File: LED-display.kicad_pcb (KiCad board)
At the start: 2 copper layers, 96.5 x 49.5 mm, 85 parts, among them J1 Conn_01x01_Male, J10 Conn_01x01_Male, J11 Conn_01x01_Male, J12 Conn_01x01_Male, J13 Conn_01x01_Male, J14 Conn_01x01_Male, J2 Conn_01x01_Male, J3 Conn_01x01_Male, J4 Conn_01x01_Male, J5 Conn_01x01_Male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

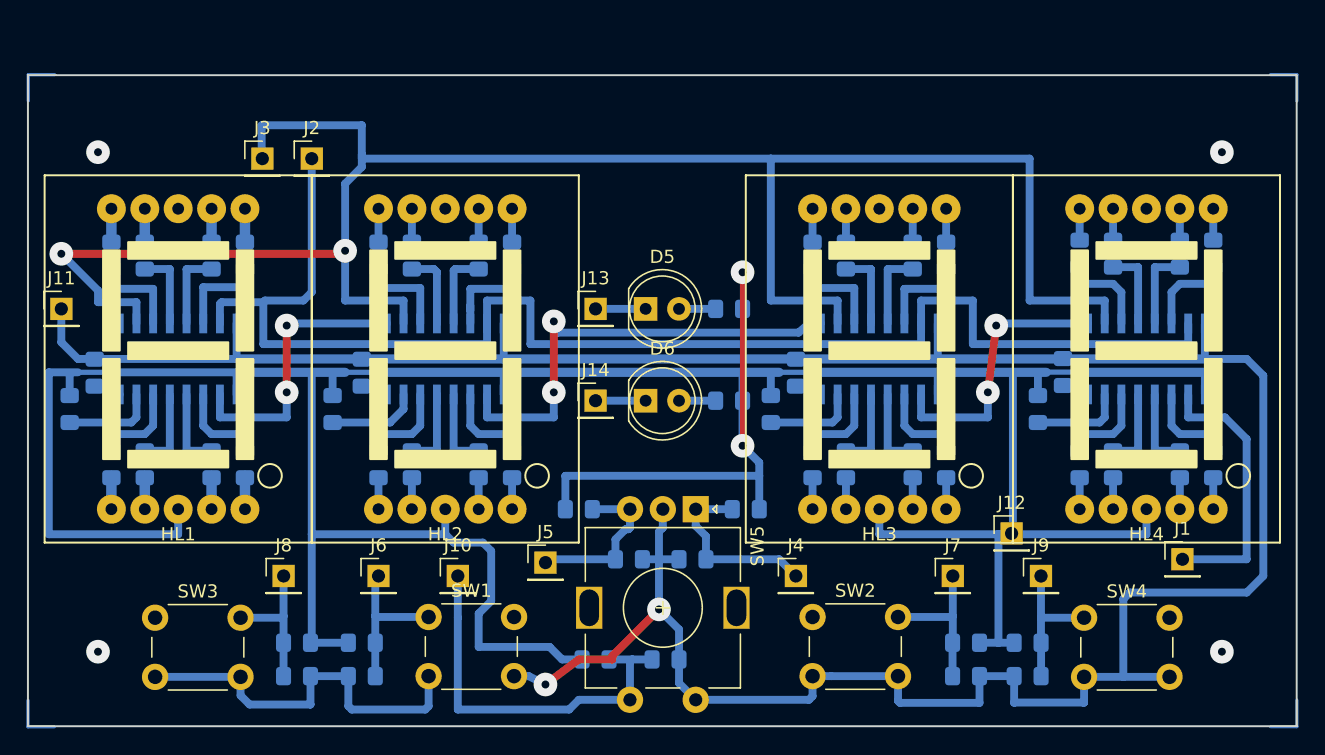
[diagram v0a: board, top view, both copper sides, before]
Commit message: Move buttons
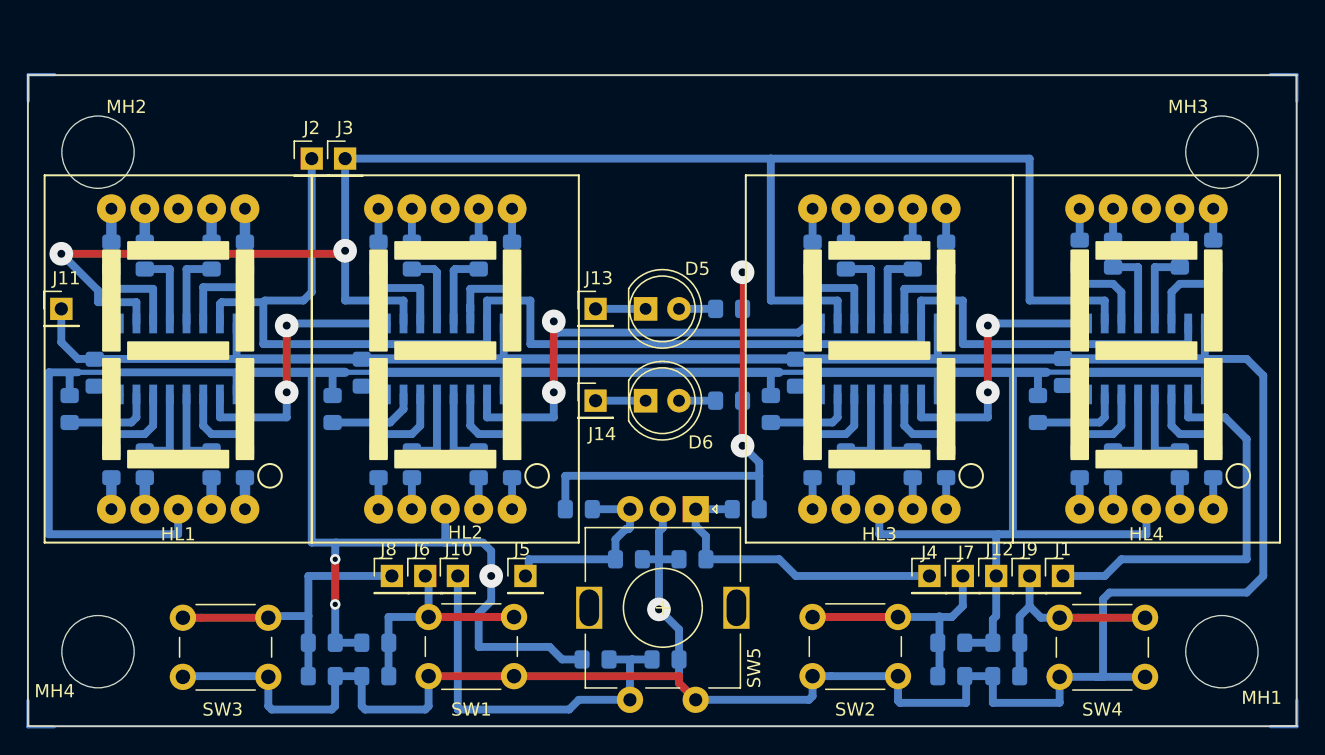
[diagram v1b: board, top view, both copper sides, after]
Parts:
- added MH1: MountingHole, MountingHole:MountingHole_5.5mm, F.Cu at (181.0, 84.5)
- added MH2: MountingHole, MountingHole:MountingHole_5.5mm, F.Cu at (95.5, 46.5)
- added MH3: MountingHole, MountingHole:MountingHole_5.5mm, F.Cu at (181.0, 46.5)
- added MH4: MountingHole, MountingHole:MountingHole_5.5mm, F.Cu at (95.5, 84.5)
- moved J4 10.2 mm to (158.8, 78.7)
- moved J1 9.18 mm to (168.9, 78.7)
- moved J8 8.23 mm to (117.9, 78.7)
- moved J3 6.30 mm to (114.3, 47.0)
- moved J6 3.56 mm to (120.4, 78.7)
- moved J12 3.44 mm to (163.8, 78.7)
- moved SW3 2.11 mm to (102.0, 81.9)
- moved C5 1.88 mm to (112.5, 86.4)
- moved R41 1.88 mm to (112.5, 83.8)
- moved SW4 1.86 mm to (168.7, 81.9)
- moved J5 1.83 mm to (128.0, 78.7)
- moved C6 1.63 mm to (164.6, 86.4)
- moved R42 1.62 mm to (164.6, 83.8)
- moved C4 1.12 mm to (160.4, 86.4)
- moved R40 1.12 mm to (160.4, 83.8)
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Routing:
- net /Zoom: track 10.9 -> 23.8 mm
- net /Latch: track 148.3 -> 136.0 mm
- net /Plus: track 14.3 -> 24.4 mm
- net /Data: track 20.9 -> 30.5 mm
- net /Min: track 11.8 -> 18.6 mm
- net /Rsrv: track 10.9 -> 17.1 mm
- net GND: track 245.6 -> 251.6 mm, vias 2 -> 1
- net /Hour: track 11.8 -> 17.2 mm
- net /Minus: track 12.6 -> 15.1 mm
- net VCC: track 272.9 -> 271.6 mm, vias 2 -> 5
- net Net-(D3-Pad2): track 20.9 -> 21.7 mm
- net (no net): vias 4 -> 0

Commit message: Small fixes
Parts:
- removed R46, R47, R48, R49: 0, Resistor_SMD:R_0805_2012Metric_Pad1.15x1.40mm_HandSolder
- added J15: PWM, Connector_PinHeader_2.54mm:PinHeader_1x01_P2.54mm_Vertical, F.Cu at (127.0, 44.5)
- J1: value Conn_01x01_Male -> Data
- J11: value Conn_01x01_Male -> Gnd
- J12: value Conn_01x01_Male -> Vcc
- J2: value Conn_01x01_Male -> Clock
- J3: value Conn_01x01_Male -> Latch
- R44, R45: moved to F.Cu
- moved J14 21.3 mm to (129.5, 44.5)
- moved J13 14.0 mm to (132.1, 44.5)
- moved J8 7.37 mm to (110.5, 78.7)
- moved J6 4.83 mm to (115.6, 78.7)
- moved R43 4.07 mm to (130.2, 87.6), turned to 270 degrees
- moved R44 2.29 mm to (142.2, 60.3), turned to 90 degrees
- moved J5 2.29 mm to (125.7, 78.7)
- moved J10 2.22 mm to (120.7, 78.7)
- moved R45 1.42 mm to (142.2, 64.8), turned to 270 degrees
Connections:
- D1 pad 8: Net-(D1-Pad8) -> /PWM
- D2 pad 8: Net-(D2-Pad8) -> /PWM
- D3 pad 8: Net-(D3-Pad8) -> /PWM
- D4 pad 8: Net-(D4-Pad8) -> /PWM
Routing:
- net /PWM: track 0.00 -> 114.8 mm, vias 0 -> 4
- net /Dot2: track 3.81 -> 25.1 mm
- net VCC: track 271.6 -> 252.4 mm, vias 5 -> 6
- net /Dot1: track 3.81 -> 16.1 mm
- net /Zoom: track 23.8 -> 17.2 mm
- net Net-(D4-Pad8): track 2.04 -> 0.00 mm
- net Net-(D2-Pad8): track 2.01 -> 0.00 mm
- net Net-(D1-Pad8): track 2.01 -> 0.00 mm
- net Net-(D3-Pad8): track 1.92 -> 0.00 mm
- net /Minus: track 15.1 -> 16.9 mm
- net GND: track 251.6 -> 249.8 mm, vias 1 -> 0
- net /Hour: track 17.2 -> 18.9 mm
- net /Valc: track 30.0 -> 29.2 mm

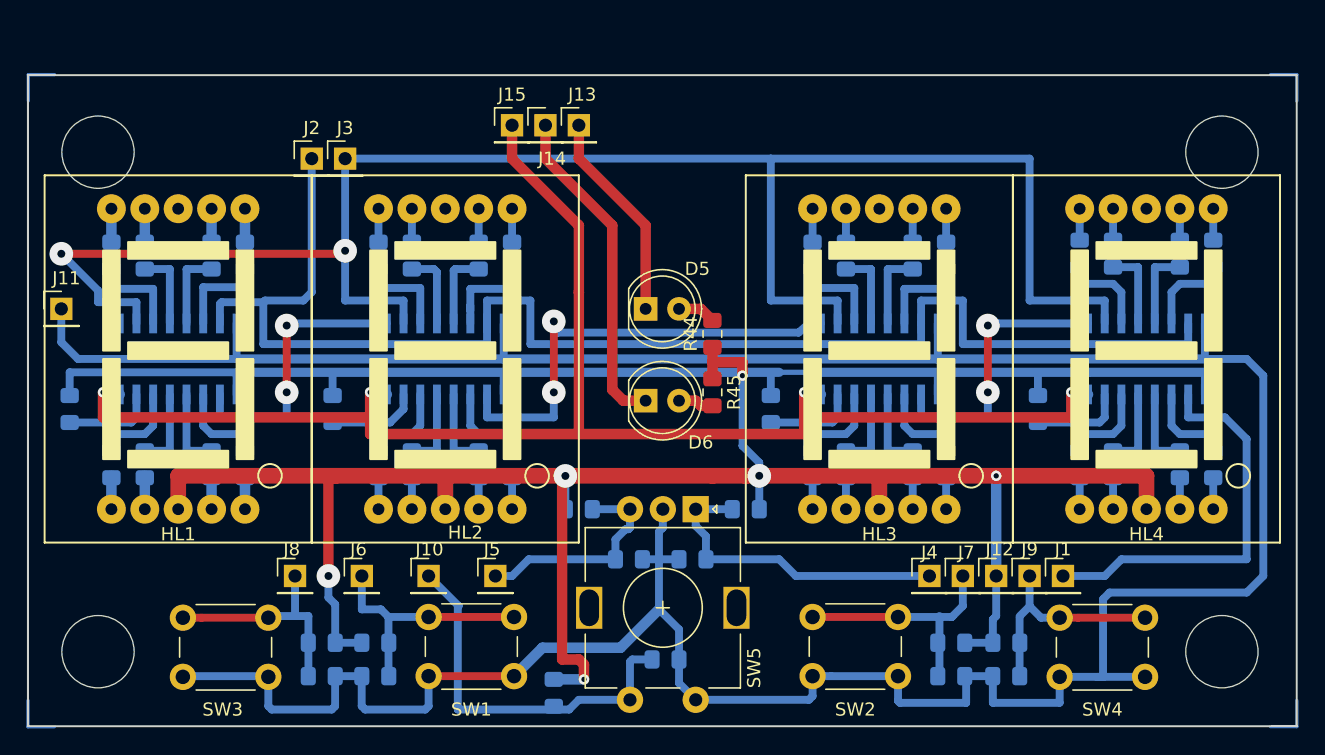
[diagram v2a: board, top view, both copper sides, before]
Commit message: Move holes and edge
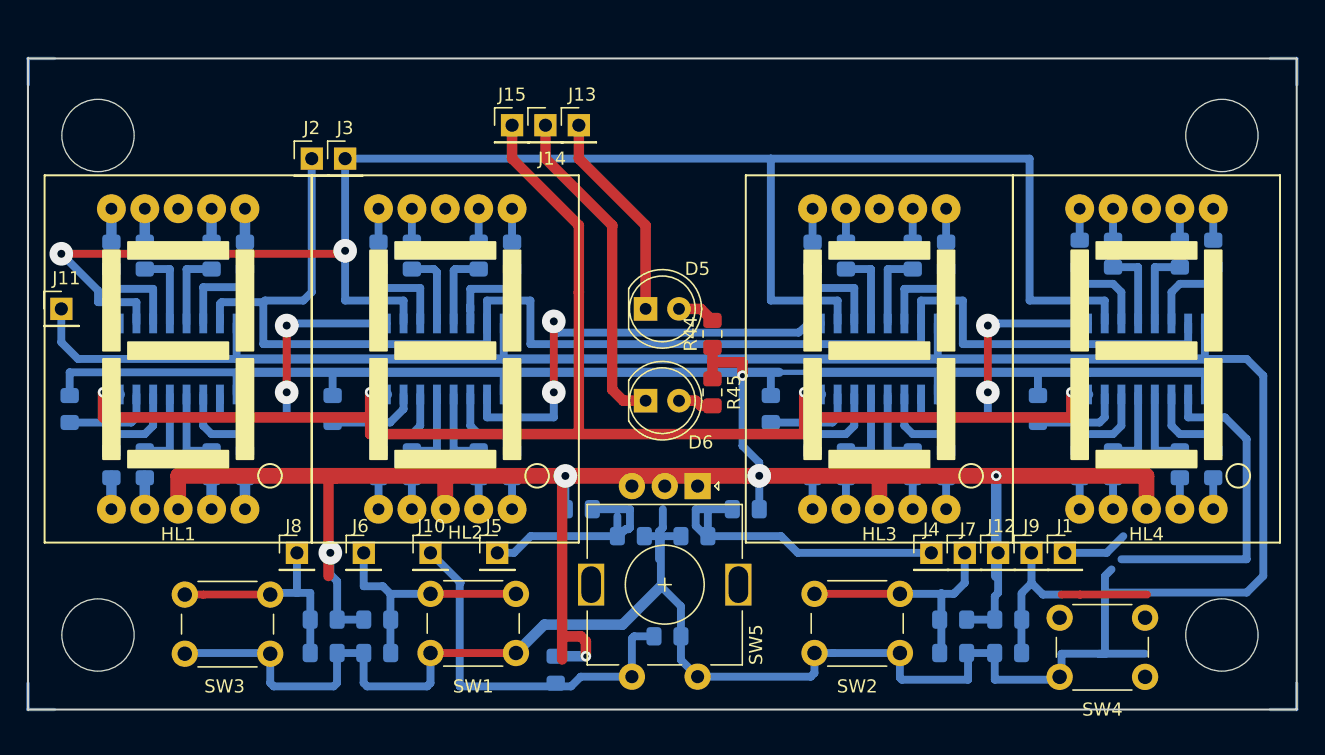
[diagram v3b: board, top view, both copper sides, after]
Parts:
- moved C1 1.77 mm to (140.9, 75.7)
- moved C2 1.77 mm to (136.0, 75.7)
- moved C4 1.77 mm to (160.6, 84.6)
- moved C3 1.77 mm to (116.7, 84.6)
- moved C5 1.77 mm to (112.7, 84.6)
- moved SW1 1.77 mm to (120.8, 80.1)
- moved SW3 1.77 mm to (102.1, 80.2)
- moved C6 1.77 mm to (164.7, 84.6)
- moved C7 1.77 mm to (138.8, 83.3)
- moved SW2 1.77 mm to (150.0, 80.1)
- moved J1 1.77 mm to (169.1, 77.0)
- moved J4 1.77 mm to (158.9, 77.0)
- moved J6 1.77 mm to (115.7, 77.0)
- moved J7 1.77 mm to (161.4, 77.0)
- moved J8 1.77 mm to (110.6, 77.0)
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
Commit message: Ready?
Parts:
- moved J11 23.8 mm to (107.7, 77.0)
- moved J3 13.0 mm to (127.0, 44.5)
- moved J2 13.0 mm to (124.5, 44.5)
- moved J15 7.62 mm to (134.6, 44.5)
- moved R2 2.17 mm to (113.7, 68.2), turned to 270 degrees
- moved R3 2.15 mm to (146.7, 68.2), turned to 270 degrees
- moved R1 2.15 mm to (94.0, 68.1), turned to 270 degrees
- moved R4 2.05 mm to (167.0, 68.1), turned to 270 degrees
- moved SW4 1.91 mm to (168.7, 80.0)
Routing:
- net VCC: track 252.4 -> 206.8 mm, vias 6 -> 12
- net /Clock: track 107.3 -> 121.5 mm
- net /PWM: track 114.8 -> 108.3 mm, vias 4 -> 1
- net /Latch: track 136.0 -> 138.5 mm
- net GND: track 249.8 -> 247.7 mm
- net /Data: track 30.5 -> 29.4 mm
- net Net-(D1-Pad7): track 6.99 -> 6.35 mm
- net /Plus: track 24.4 -> 23.8 mm
- net /Minus: track 16.9 -> 16.4 mm
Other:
- board text added: "Clk"
- board text added: "D"
- board text added: "D1"
- board text added: "D2"
- board text added: "Gnd"
- board text added: "H"
- board text added: "L"
- board text added: "M"
- board text added: "M-"
- board text added: "P+"
- board text added: "PWM"
- board text added: "R"
- board text added: "V"
- board text added: "Vcc"
- board text added: "Z"

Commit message: Now it's double side pcb
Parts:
- added J16: Conn_01x01_Male, Connector_PinHeader_2.54mm:PinHeader_1x01_P2.54mm_Vertical, F.Cu at (137.2, 44.5)
- added R46: R, Resistor_SMD:R_0805_2012Metric_Pad1.15x1.40mm_HandSolder, F.Cu at (144.8, 48.3)
- added R47: R_PHOTO, OptoDevice:R_LDR_4.9x4.2mm_P2.54mm_Vertical, F.Cu at (144.8, 44.5)
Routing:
- net (no net): track 16.0 -> 163.8 mm
- net GND: track 247.7 -> 279.4 mm, vias 0 -> 1
- net VCC: track 206.8 -> 230.7 mm
- net Net-(J16-Pad1): track 0.00 -> 10.4 mm
- net /PWM: track 108.3 -> 106.4 mm
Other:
- board text added: "23.07.2019"
- board text added: "JustMoose"

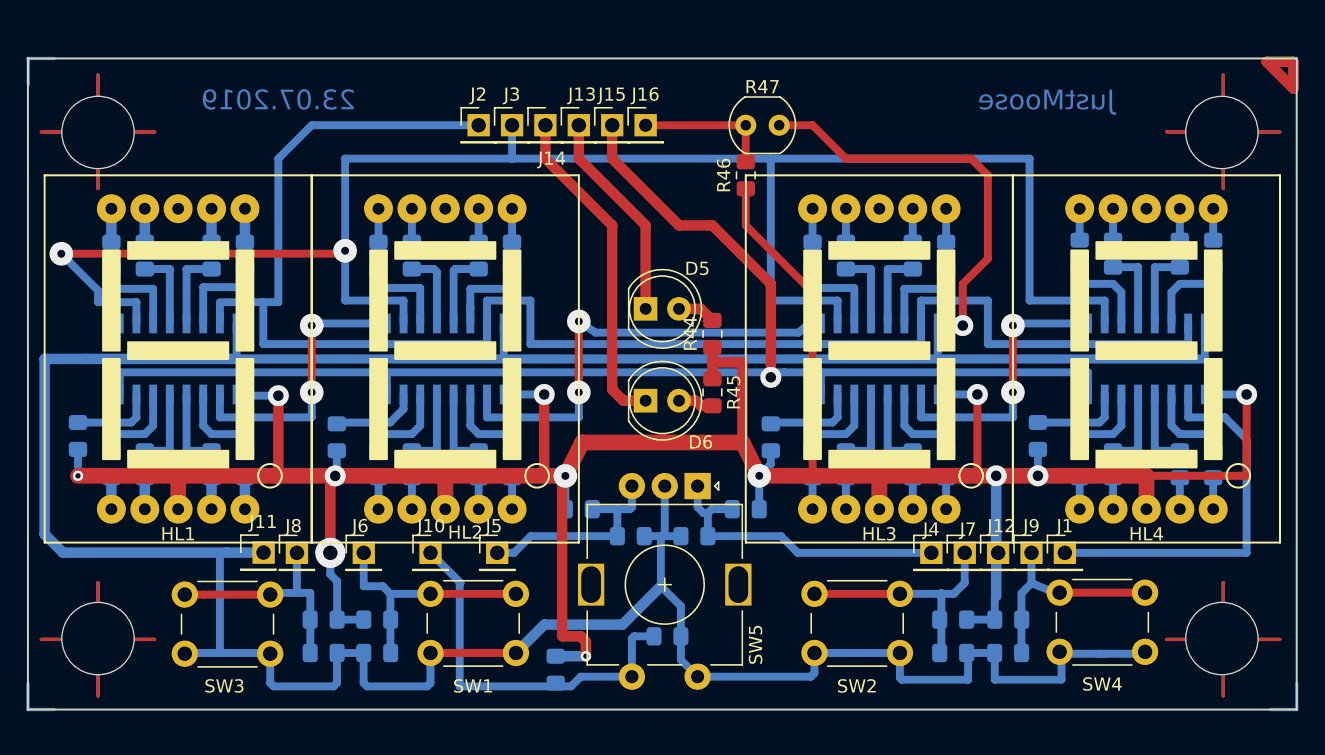
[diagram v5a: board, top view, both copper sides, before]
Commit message: Enlarge holes and pads. Fix pinheader pos.
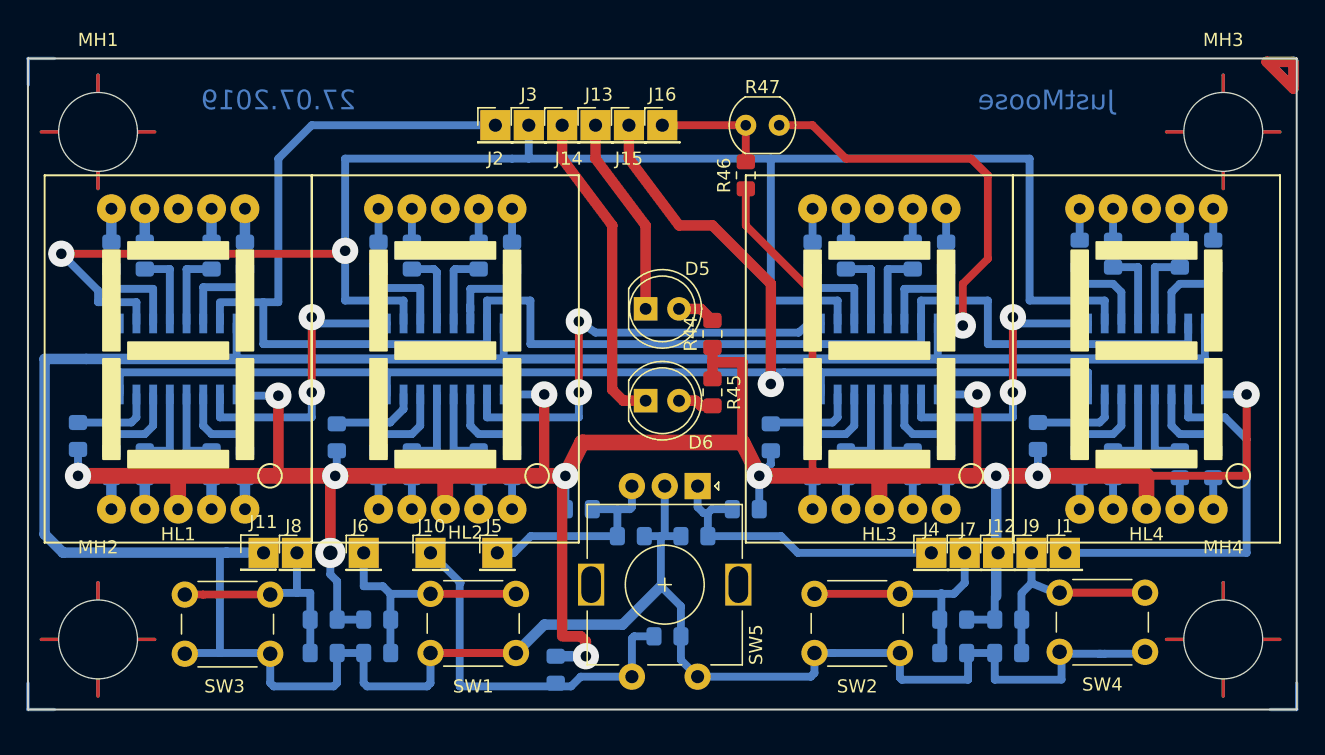
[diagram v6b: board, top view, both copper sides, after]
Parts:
- MH1, MH2, MH3, MH4: footprint MountingHole:MountingHole_5.5mm -> MountingHole:MountingHole_6mm
- moved MH1 93.7 mm to (95.5, 45.0)
- moved MH4 85.6 mm to (181.1, 83.6)
- moved MH2 38.3 mm to (95.5, 83.6)
- moved J14 1.27 mm to (130.8, 44.5)
- moved J16 1.27 mm to (138.4, 44.5)
- moved J2 1.27 mm to (125.7, 44.5)
- moved J3 1.27 mm to (128.3, 44.5)
- moved J13 1.27 mm to (133.3, 44.5)
- moved J15 1.27 mm to (135.9, 44.5)
- moved MH3 0.29 mm to (181.1, 45.0)
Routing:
- net Net-(J16-Pad1): track 10.4 -> 9.13 mm
- net /Clock: track 121.5 -> 122.8 mm
- net /Dot2: track 25.1 -> 24.3 mm
- net /Dot1: track 16.1 -> 15.2 mm
- net Net-(D3-Pad2): track 21.4 -> 22.1 mm
- net Net-(D1-Pad2): track 21.4 -> 22.1 mm
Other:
- board text added: "27.07.2019"
- board text added: "Light"
- board text removed: "23.07.2019"
